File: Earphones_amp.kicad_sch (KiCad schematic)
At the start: 48 parts, among them J1 AudioJack3, Q1 2SC1815, Q2 2SA1015, Q3 PNP, Q4 NPN, Q5 NPN, Q6 PNP, U1 LM358, U2 ${SIM.PARAMS}, U3 Opamp_Dual, U4 Opamp_Dual, U5 Opamp_Dual, U6 Opamp_Dual, U7 Opamp_Dual

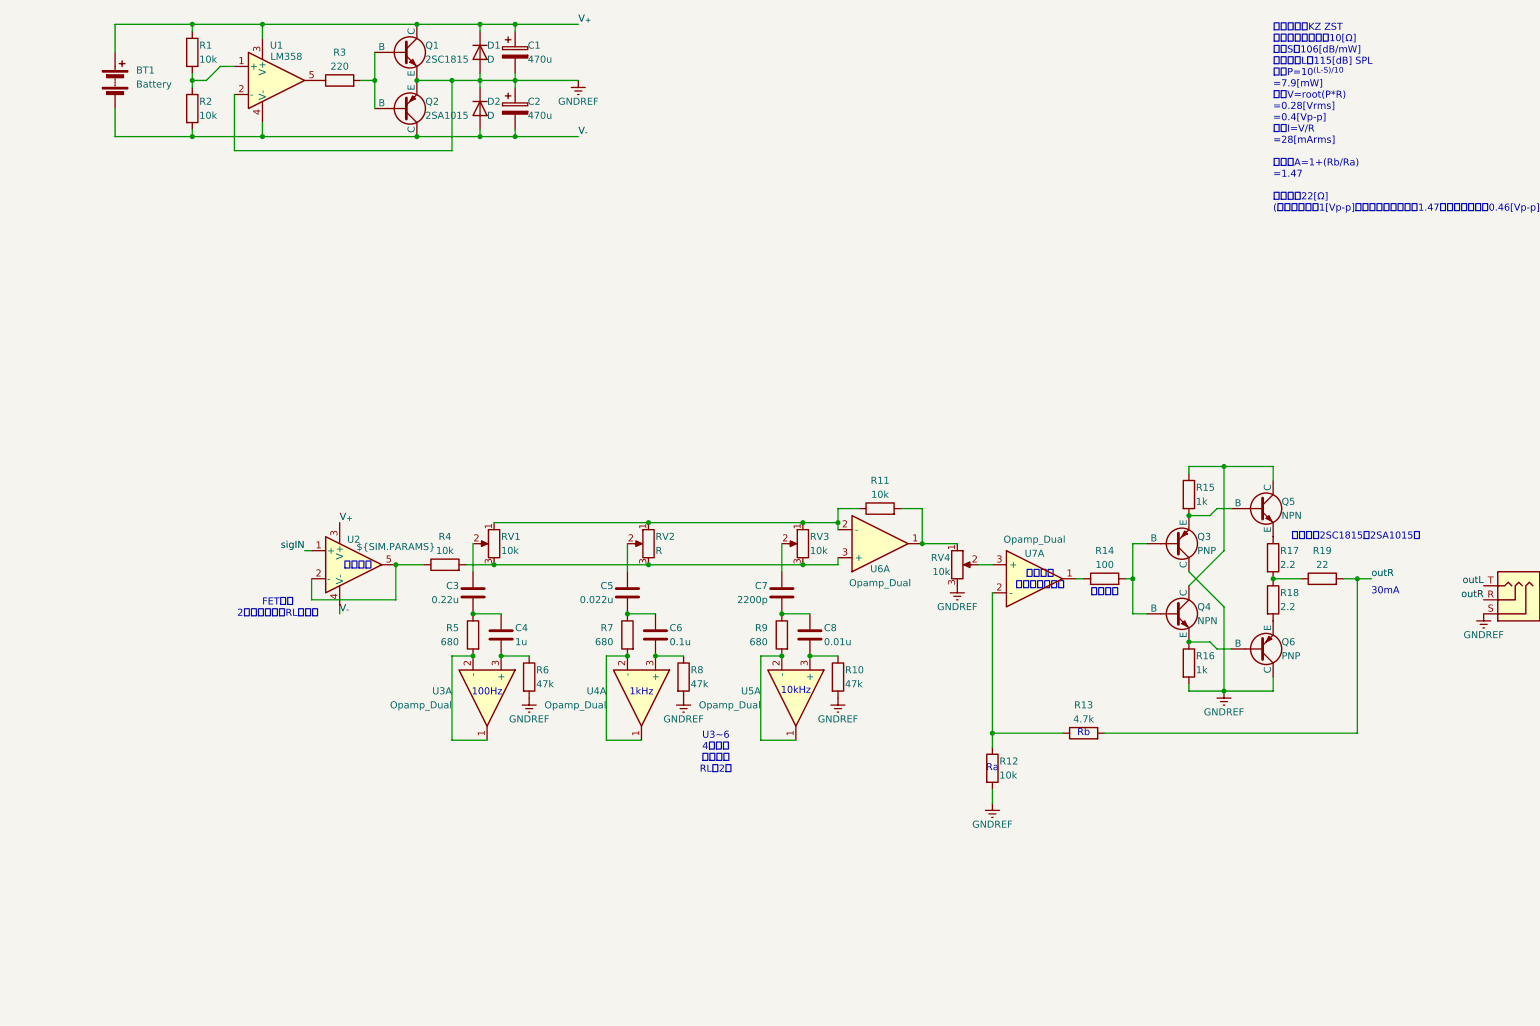
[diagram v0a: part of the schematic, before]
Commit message: 回路図Done LT->DT
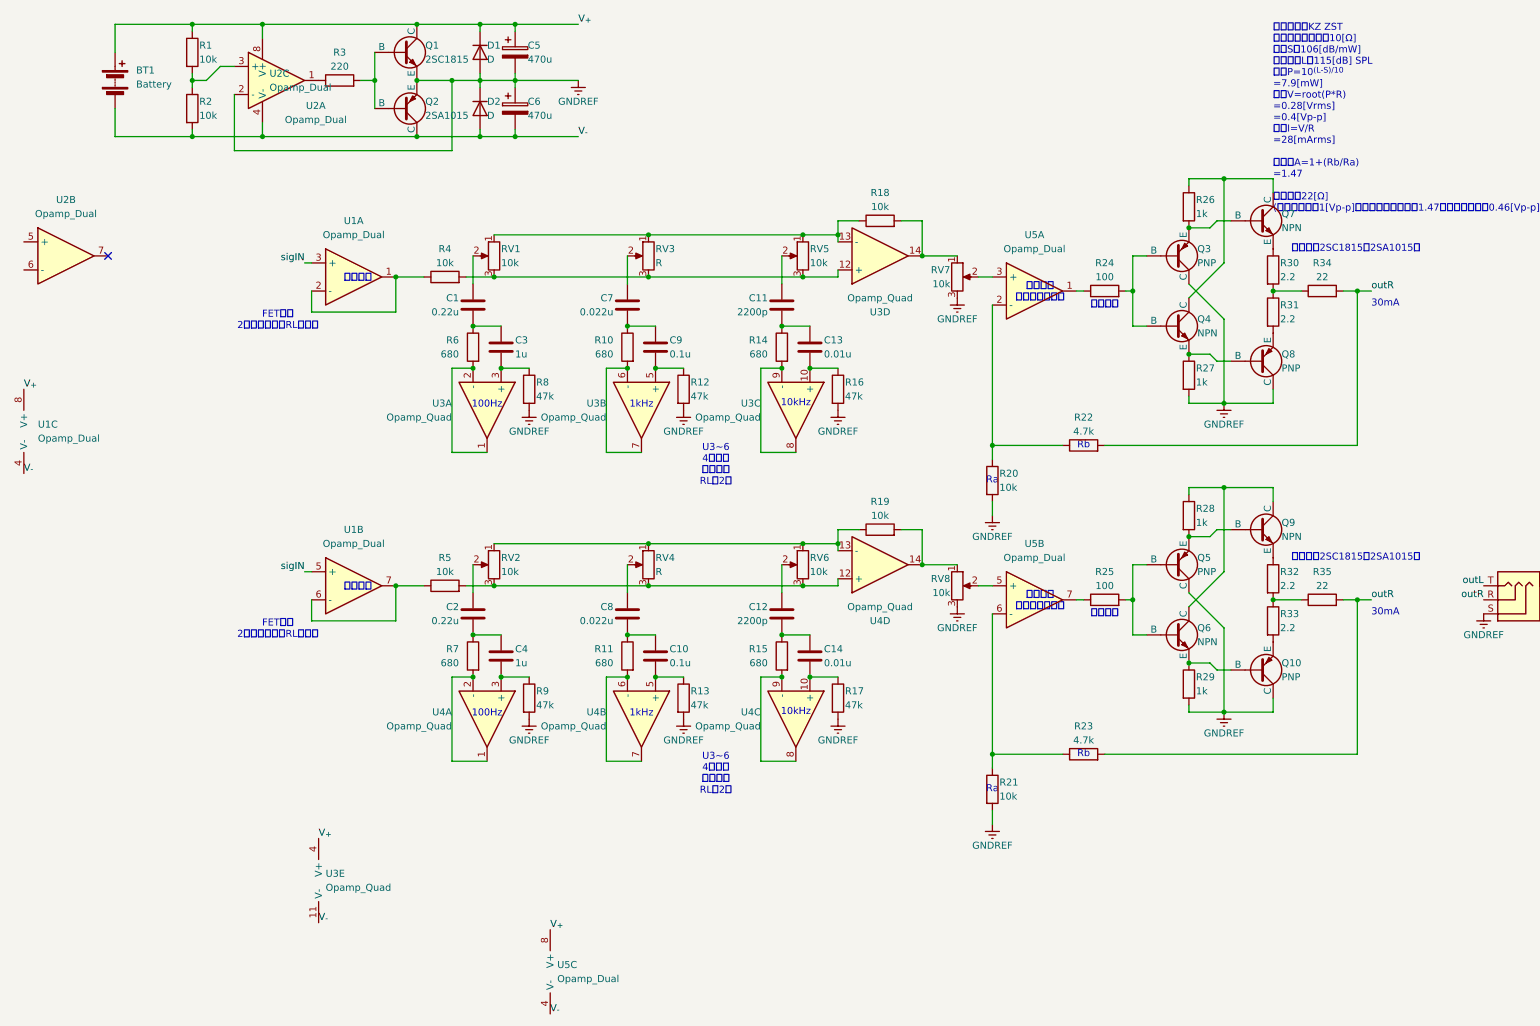
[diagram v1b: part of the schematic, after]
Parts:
- removed U1: LM358, symbol Simulation_SPICE:OPAMP
- removed U2: ${SIM.PARAMS}, symbol Simulation_SPICE:OPAMP
- removed U3, U4, U6, U7: Opamp_Dual, symbol Device:Opamp_Dual
- added C10: 0.1u, symbol Device:C
- added C12: 2200p, symbol Device:C
- added C14: 0.01u, symbol Device:C
- added C2: 0.22u, symbol Device:C
- added C4: 1u, symbol Device:C
- added C8: 0.022u, symbol Device:C
- added Q10, Q5: PNP, Package_TO_SOT_THT:TO-92L_Inline_Wide, symbol Simulation_SPICE:PNP
- added Q6, Q9: NPN, Package_TO_SOT_THT:TO-92L_Inline_Wide, symbol Simulation_SPICE:NPN
- added R11, R15, R7: 680, Resistor_THT:R_Axial_DIN0204_L3.6mm_D1.6mm_P5.08mm_Horizontal, symbol Device:R
- added R13, R17, R9: 47k, Resistor_THT:R_Axial_DIN0204_L3.6mm_D1.6mm_P5.08mm_Horizontal, symbol Device:R
- added R19, R21, R5: 10k, Resistor_THT:R_Axial_DIN0204_L3.6mm_D1.6mm_P5.08mm_Horizontal, symbol Device:R
- added R23: 4.7k, Resistor_THT:R_Axial_DIN0204_L3.6mm_D1.6mm_P5.08mm_Horizontal, symbol Device:R
- added R25: 100, Resistor_THT:R_Axial_DIN0204_L3.6mm_D1.6mm_P5.08mm_Horizontal, symbol Device:R
- added R28, R29: 1k, Resistor_THT:R_Axial_DIN0204_L3.6mm_D1.6mm_P5.08mm_Horizontal, symbol Device:R
- added R32, R33: 2.2, Resistor_THT:R_Axial_DIN0207_L6.3mm_D2.5mm_P7.62mm_Horizontal, symbol Device:R
- added R35: 22, Resistor_THT:R_Axial_DIN0204_L3.6mm_D1.6mm_P5.08mm_Horizontal, symbol Device:R
- added RV2, RV6, RV8: 10k, symbol Device:R_Potentiometer
- added RV4: R, symbol Device:R_Potentiometer
- added U1, U2: Opamp_Dual, symbol Device:Opamp_Dual
- added U3, U4: Opamp_Quad, symbol Device:Opamp_Quad
- added unit 2 of U5
- added unit 3 of U5
- BT1: footprint (none) -> Connector_JST:JST_XH_B2B-XH-AM_1x02_P2.50mm_Vertical
- C5: renamed from C1; footprint (none) -> Capacitor_THT:CP_Radial_D16.0mm_P7.50mm
- C6: renamed from C2; footprint (none) -> Capacitor_THT:CP_Radial_D16.0mm_P7.50mm
- D1, D2: footprint (none) -> Diode_THT:D_DO-35_SOD27_P7.62mm_Horizontal
- Q1, Q2, Q3, Q4: footprint (none) -> Package_TO_SOT_THT:TO-92L_Inline_Wide
- Q7: renamed from Q5; footprint (none) -> Package_TO_SOT_THT:TO-92L_Inline_Wide
- Q8: renamed from Q6; footprint (none) -> Package_TO_SOT_THT:TO-92L_Inline_Wide
- R1, R2, R3, R4: footprint (none) -> Resistor_THT:R_Axial_DIN0204_L3.6mm_D1.6mm_P5.08mm_Horizontal
- R10: renamed from R7; footprint (none) -> Resistor_THT:R_Axial_DIN0204_L3.6mm_D1.6mm_P5.08mm_Horizontal
- R12: renamed from R8; footprint (none) -> Resistor_THT:R_Axial_DIN0204_L3.6mm_D1.6mm_P5.08mm_Horizontal
- R14: renamed from R9; footprint (none) -> Resistor_THT:R_Axial_DIN0204_L3.6mm_D1.6mm_P5.08mm_Horizontal
- R16: renamed from R10; footprint (none) -> Resistor_THT:R_Axial_DIN0204_L3.6mm_D1.6mm_P5.08mm_Horizontal
- R18: renamed from R11; footprint (none) -> Resistor_THT:R_Axial_DIN0204_L3.6mm_D1.6mm_P5.08mm_Horizontal
- R20: renamed from R12; footprint (none) -> Resistor_THT:R_Axial_DIN0204_L3.6mm_D1.6mm_P5.08mm_Horizontal
- R22: renamed from R13; footprint (none) -> Resistor_THT:R_Axial_DIN0204_L3.6mm_D1.6mm_P5.08mm_Horizontal
- R24: renamed from R14; footprint (none) -> Resistor_THT:R_Axial_DIN0204_L3.6mm_D1.6mm_P5.08mm_Horizontal
- R26: renamed from R15; footprint (none) -> Resistor_THT:R_Axial_DIN0204_L3.6mm_D1.6mm_P5.08mm_Horizontal
- R27: renamed from R16; footprint (none) -> Resistor_THT:R_Axial_DIN0204_L3.6mm_D1.6mm_P5.08mm_Horizontal
- R30: renamed from R17; footprint (none) -> Resistor_THT:R_Axial_DIN0207_L6.3mm_D2.5mm_P7.62mm_Horizontal
- R31: renamed from R18; footprint (none) -> Resistor_THT:R_Axial_DIN0207_L6.3mm_D2.5mm_P7.62mm_Horizontal
- R34: renamed from R19; footprint (none) -> Resistor_THT:R_Axial_DIN0204_L3.6mm_D1.6mm_P5.08mm_Horizontal
- R6: renamed from R5; footprint (none) -> Resistor_THT:R_Axial_DIN0204_L3.6mm_D1.6mm_P5.08mm_Horizontal
- R8: renamed from R6; footprint (none) -> Resistor_THT:R_Axial_DIN0204_L3.6mm_D1.6mm_P5.08mm_Horizontal
- renumbered C3 to C1, C7 to C11, C8 to C13, C4 to C3, C5 to C7, C6 to C9, RV2 to RV3, RV3 to RV5, RV4 to RV7
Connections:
- net GNDREF: now also Q10.1 (C), Q5.1 (C), R13.2, R17.2, R21.2, R29.2, R9.2, RV8.3, U2.2 (-)
- net V_{+}: now also U1.8 (V+), U2.8 (V+), U3.4 (V+), U5.8 (V+)
- net V_{-}: now also U1.4 (V-), U2.4 (V-), U3.11 (V-), U5.4 (V-)
- net outR: now also R23.2, R35.2
- net sigIN: now also U1.3 (+), U1.5 (+)
- net at C13.2, R16.1: now also U3.10 (+); no longer U5.3 (+)
- net at R6.2: now also U3.1, U3.2 (-)
- net at R20.1, R22.1: now also U5.2 (-)
- net at C3.2, R8.1: now also U3.3 (+)
- net at R18.1, RV1.1, RV3.1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: now also U3.13 (-)
- net at R18.2, RV7.1: now also U3.14
- net at RV7.2: now also U5.3 (+)
- net at R1.2, R2.1: now also U2.3 (+)
- net at C9.2, R12.1: now also U3.5 (+)
- net at R10.2: now also U3.6 (-), U3.7
- net at R3.1: now also U2.1
- net at R4.2, RV1.3, RV3.3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: now also U3.12 (+)
- net at R4.1: now also U1.1, U1.2 (-)
- net at R24.1: now also U5.1
- new net: C14.2, R17.1, U4.10 (+)
- new net: R15.2, U4.8, U4.9 (-)
- new net: R19.1, RV2.1, RV4.1, RV6.1, U4.13 (-)
- new net: C2.1, RV2.2
- new net: R5.2, RV2.3, RV4.3, RV6.3, U4.12 (+)
- new net: C10.1, C8.2, R11.1
- new net: C10.2, R13.1, U4.5 (+)
- new net: R11.2, U4.6 (-), U4.7
- new net: R14.2, U3.8, U3.9 (-)
- new net: C12.1, RV6.2
- new net: C12.2, C14.1, R15.1
- new net: R25.1, U5.7
- new net: Q5.2 (B), Q6.2 (B), R25.2
- new net: Q10.2 (B), Q6.3 (E), R29.1
- new net: C4.2, R9.1, U4.3 (+)
- new net: R19.2, RV8.1, U4.14
- new net: Q6.1 (C), Q9.1 (C), R28.1
- new net: Q5.3 (E), Q9.2 (B), R28.2
- new net: Q9.3 (E), R32.1
- new net: C8.1, RV4.2
- new net: R21.1, R23.1, U5.6 (-)
- new net: R5.1, U1.6 (-), U1.7
- new net: RV8.2, U5.5 (+)
- new net: R32.2, R33.1, R35.1
- new net: Q10.3 (E), R33.2
- new net: R7.2, U4.1, U4.2 (-)
- new net: C2.2, C4.1, R7.1
- no-connect marks 0 -> 1
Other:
- moved on the sheet: C1, C11, C13, C3, C7, C9, Q3, Q4, Q7, Q8, R10, R12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

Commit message: 部品紐づけ進めた
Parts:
- U1, U2, U5: footprint (none) -> Package_DIP:DIP-8_W7.62mm_Socket
- U3, U4: footprint (none) -> Package_DIP:DIP-14_W7.62mm_Socket
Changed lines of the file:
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@@
 			)
 		)
-		(property "Footprint" ""
+		(property "Footprint" "Package_DIP:DIP-14_W7.62mm_Socket"
 			(at 138.43 140.97 0)
 			(effects
@@
 			)
 		)
-		(property "Footprint" ""
+		(property "Footprint" "Package_DIP:DIP-8_W7.62mm_Socket"
 			(at 44.45 25.4 0)
 			(effects
@@
 			)
 		)
-		(property "Footprint" ""
+		(property "Footprint" "Package_DIP:DIP-14_W7.62mm_Socket"
 			(at 110.49 140.97 0)
 			(effects
@@
 			)
 		)
-		(property "Footprint" ""
+		(property "Footprint" "Package_DIP:DIP-14_W7.62mm_Socket"
 			(at 138.43 85.09 0)
 			(effects
@@
 			)
 		)
-		(property "Footprint" ""
+		(property "Footprint" "Package_DIP:DIP-14_W7.62mm_Socket"
 			(at 153.67 57.15 0)
 			(effects
@@
 			)
 		)
-		(property "Footprint" ""
+		(property "Footprint" "Package_DIP:DIP-14_W7.62mm_Socket"
 			(at 153.67 113.03 0)
 			(effects
@@
 			)
 		)
-		(property "Footprint" ""
+		(property "Footprint" "Package_DIP:DIP-14_W7.62mm_Socket"
 			(at 54.61 170.18 0)
 			(effects
@@
 			)
 		)
-		(property "Footprint" ""
+		(property "Footprint" "Package_DIP:DIP-14_W7.62mm_Socket"
 			(at 82.55 85.09 0)
 			(effects
@@
 			)
 		)
-		(property "Footprint" ""
+		(property "Footprint" "Package_DIP:DIP-8_W7.62mm_Socket"
 			(at 58.42 116.84 0)
 			(effects
@@
 			)
 		)
-		(property "Footprint" ""
+		(property "Footprint" "Package_DIP:DIP-8_W7.62mm_Socket"
 			(at 1.27 88.9 0)
 			(effects
@@
 			)
 		)
-		(property "Footprint" ""
+		(property "Footprint" "Package_DIP:DIP-8_W7.62mm_Socket"
 			(at 181.61 119.38 0)
 			(effects
@@
 			)
 		)
-		(property "Footprint" ""
+		(property "Footprint" "Package_DIP:DIP-8_W7.62mm_Socket"
 			(at 58.42 60.96 0)
 			(effects
@@
 			)
 		)
-		(property "Footprint" ""
+		(property "Footprint" "Package_DIP:DIP-14_W7.62mm_Socket"
 			(at 82.55 140.97 0)
 			(effects
@@
 			)
 		)
-		(property "Footprint" ""
+		(property "Footprint" "Package_DIP:DIP-8_W7.62mm_Socket"
 			(at 44.45 25.4 0)
 			(effects
@@
 			)
 		)
-		(property "Footprint" ""
+		(property "Footprint" "Package_DIP:DIP-8_W7.62mm_Socket"
 			(at 181.61 63.5 0)
 			(effects
@@
 			)
 		)
-		(property "Footprint" ""
+		(property "Footprint" "Package_DIP:DIP-8_W7.62mm_Socket"
 			(at 6.35 57.15 0)
 			(effects
@@
 			)
 		)
-		(property "Footprint" ""
+		(property "Footprint" "Package_DIP:DIP-14_W7.62mm_Socket"
 			(at 110.49 85.09 0)
 			(effects
@@
 			)
 		)
-		(property "Footprint" ""
+		(property "Footprint" "Package_DIP:DIP-8_W7.62mm_Socket"
 			(at 96.52 186.69 0)
 			(effects

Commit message: 回路図完成
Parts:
- removed Q10, Q3, Q5, Q8: PNP, Package_TO_SOT_THT:TO-92L_Inline_Wide, symbol Simulation_SPICE:PNP
- removed Q4, Q6, Q7, Q9: NPN, Package_TO_SOT_THT:TO-92L_Inline_Wide, symbol Simulation_SPICE:NPN
- removed RV1, RV2, RV5, RV6, RV7, RV8: 10k, symbol Device:R_Potentiometer
- removed RV3, RV4: R, symbol Device:R_Potentiometer
- added D1: LED, LED_THT:LED_D5.0mm, symbol Device:LED
- added J1: AudioJack3, MyLibrary:MJ352W, symbol Connector_Audio:AudioJack3
- added Q10, Q3, Q5, Q8: PNP, Package_TO_SOT_THT:TO-92L_Inline_Wide, symbol Transistor_BJT:Q_PNP_ECB
- added Q4, Q6, Q7, Q9: NPN, Package_TO_SOT_THT:TO-92L_Inline_Wide, symbol Transistor_BJT:Q_NPN_ECB
- added R1: 2k, Resistor_THT:R_Axial_DIN0204_L3.6mm_D1.6mm_P5.08mm_Horizontal, symbol Device:R
- added RV1, RV2, RV3: 10k, samacsys:SL4515NB103L15CM, symbol MysymbolLibrary:RV_2C
- added RV4: 50k, MyLibrary:RV_2C, symbol MysymbolLibrary:RV_2C
- added unit 5 of U5
- BT1: value Battery -> 9V; footprint Connector_JST:JST_XH_B2B-XH-AM_1x02_P2.50mm_Vertical -> Connector_JST:JST_XH_S2B-XH-A_1x02_P2.50mm_Horizontal
- C10, C11, C12, C13, C14, C7, C8, C9: footprint (none) -> Capacitor_THT:C_Rect_L7.2mm_W2.5mm_P5.00mm
- C3: renamed from C1; footprint (none) -> Capacitor_THT:C_Rect_L7.2mm_W3.5mm_P5.00mm
- C4: renamed from C2; footprint (none) -> Capacitor_THT:C_Rect_L7.2mm_W3.5mm_P5.00mm
- C5: renamed from C3; footprint (none) -> Capacitor_THT:C_Rect_L7.2mm_W6.0mm_P5.00mm
- C6: renamed from C4; footprint (none) -> Capacitor_THT:C_Rect_L7.2mm_W6.0mm_P5.00mm
- J2: renamed from J1; footprint (none) -> MyLibrary:MJ352W
- U2: renamed from U1; value Opamp_Dual -> TL072
- U3: value Opamp_Quad -> TL074
- U4: renamed from U5; value Opamp_Dual -> OPA1655DR
- U5: renamed from U4; value Opamp_Quad -> TL074
- renumbered C5 to C1, C6 to C2, D1 to D2, D2 to D3, R9 to R10, R10 to R11, R11 to R12, R12 to R13, R13 to R14, R14 to R15, R15 to R16, R16 to R17, R17 to R18, R18 to R19, R1 to R2, R19 to R20, R20 to R21, R21 to R22, R22 to R23, R23 to R24, R24 to R25, R25 to R26, R26 to R27, R27 to R28, R28 to R29, R2 to R3, R29 to R30, R30 to R31, R31 to R32, R32 to R33, R33 to R34, R34 to R35, R35 to R36, R3 to R4, R4 to R5, R5 to R6, R6 to R7, R7 to R8, R8 to R9, U2 to U1
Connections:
- net GNDREF: now also U1.5 (+), J1.S, RV4.3, RV4.6; no longer R28.2, R30.2
- net V_{+}: now also R27.1, R29.1, D1.2 (A), Q4.2 (C), Q6.2 (C), Q7.2 (C), Q9.2 (C), U5.11 (V-), U5.4 (V+)
- net V_{-}: now also R28.2, R30.2, Q10.1 (E), Q3.1 (E), Q5.1 (E), Q8.1 (E), R1.2
- net at R20.1, U5.13 (-): now also RV1.4, RV2.4, RV3.4
- net at C4.1: now also RV1.5
- net at R6.2, U5.12 (+): now also RV1.6, RV2.6, RV3.6
- net at R27.2: now also Q3.2 (C), Q7.3 (B)
- net at R31.1: now also Q7.1 (E)
- net at R32.2: now also Q8.2 (C)
- net at C12.1: now also RV3.5
- net at R26.2: now also Q5.3 (B), Q6.3 (B)
- net at R5.2, U3.12 (+): now also RV1.3, RV2.3, RV3.3
- net at R19.1, U3.13 (-): now also RV1.1, RV2.1, RV3.1
- net at R19.2, U3.14: now also RV4.1
- net at R30.1: now also Q10.3 (B), Q6.1 (E)
- net at R20.2, U5.14: now also RV4.4
- net at R29.2: now also Q5.2 (C), Q9.3 (B)
- net at R33.1: now also Q9.1 (E)
- net at C7.1: now also RV2.2
- net at U4.3 (+): now also RV4.2
- net at C8.1: now also RV2.5
- net at U4.5 (+): now also RV4.5
- net at C3.1: now also RV1.2
- net at R34.2: now also Q10.2 (C)
- net at R28.1: now also Q4.1 (E), Q8.3 (B)
- net at R25.2: now also Q3.3 (B), Q4.3 (B)
- net at C11.1: now also RV3.2
- net at U1.6 (-): now also U1.7
- net sigIN renamed sigIN_L
- net sigIN_L: now also J1.T; no longer U2.3 (+)
- new net: D1.1 (K), R1.1
- new net sigIN_R: J1.R, U2.3 (+)
- no-connect marks 1 -> 0
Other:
- note removed: "いったん2SC1815と2SA1015で"
- moved on the sheet: BT1, C1, C2, D2, D3, J2, Q1, Q2, R2, R3, R4, U1A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

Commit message: PCBすすめた
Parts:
- RV1, RV2, RV3: footprint samacsys:SL4515NB103L15CM -> MyLibrary:SL4515G
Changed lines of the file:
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@@
 			)
 		)
-		(property "Footprint" "samacsys:SL4515NB103L15CM"
+		(property "Footprint" "MyLibrary:SL4515G"
 			(at 83.82 57.15 0)
 			(hide yes)
@@
 			)
 		)
-		(property "Footprint" "samacsys:SL4515NB103L15CM"
+		(property "Footprint" "MyLibrary:SL4515G"
 			(at 139.7 57.15 0)
 			(hide yes)
@@
 			)
 		)
-		(property "Footprint" "samacsys:SL4515NB103L15CM"
+		(property "Footprint" "MyLibrary:SL4515G"
 			(at 83.82 113.03 0)
 			(hide yes)
@@
 			)
 		)
-		(property "Footprint" "samacsys:SL4515NB103L15CM"
+		(property "Footprint" "MyLibrary:SL4515G"
 			(at 111.76 57.15 0)
 			(hide yes)
@@
 			)
 		)
-		(property "Footprint" "samacsys:SL4515NB103L15CM"
+		(property "Footprint" "MyLibrary:SL4515G"
 			(at 111.76 113.03 0)
 			(hide yes)
@@
 			)
 		)
-		(property "Footprint" "samacsys:SL4515NB103L15CM"
+		(property "Footprint" "MyLibrary:SL4515G"
 			(at 139.7 113.03 0)
 			(hide yes)
